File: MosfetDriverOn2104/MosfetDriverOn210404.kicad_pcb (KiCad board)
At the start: 2 copper layers, 93.5 x 94.9 mm, 88 parts, among them J1 I2C HDR, J10 ENCODER HDR, J11 CROSS CONN, J12 motor, J2 AVR-ISP-6, J3 I2C HDR, J4 Screw_Terminal_01x02, J5 I2C HDR, J6 UART HDR, J7 5V HDR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

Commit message: check
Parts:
- moved R8 29.9 mm to (198.9, 83.5)
- moved R9 28.0 mm to (194.8, 82.1)
- moved R7 26.0 mm to (192.3, 79.3)
- moved R12 25.6 mm to (189.4, 76.5)
- moved R11 25.1 mm to (186.8, 73.5)
- moved C1 2.67 mm to (122.6, 93.3)
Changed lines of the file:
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@@
   )
   (module Capacitor_SMD:CP_Elec_8x6.2 (layer F.Cu)
-    (at 125.044564 94.432498 320)
+    (at 122.631564 93.289498 320)
     (descr "SMT capacitor, aluminium electrolytic, 8x6.2, Nichicon ")
     (tags "Capacitor Electrolytic")
@@
     (pad 2 thru_hole circle (at -5.08 -6.35 235) (size 3.556 3.556) (drill 3.556) (layers *.Cu *.Mask)
       (net 8 VCC))
-    (pad 2 thru_hole circle (at 0 -6.35 235) (size 3.556 3.556) (drill 3.556) (layers *.Cu *.Mask)
+    (pad 2 thru_hole circle (at 0 -6.349999 235) (size 3.556 3.556) (drill 3.556) (layers *.Cu *.Mask)
       (net 8 VCC))
   )
@@
     (fp_line (start 5.334 -3.048) (end -5.334 -3.048) (layer F.SilkS) (width 0.15))
     (fp_line (start 5.334 0) (end 5.334 -3.048) (layer F.SilkS) (width 0.15))
-    (pad 2 thru_hole circle (at 0 -6.35 235) (size 3.556 3.556) (drill 3.556) (layers *.Cu *.Mask)
+    (pad 2 thru_hole circle (at 0 -6.349999 235) (size 3.556 3.556) (drill 3.556) (layers *.Cu *.Mask)
       (net 42 /M1))
     (pad 2 thru_hole circle (at -5.08 -6.35 235) (size 3.556 3.556) (drill 3.556) (layers *.Cu *.Mask)
@@
     (pad 2 thru_hole circle (at -5.08 -6.35 35) (size 3.556 3.556) (drill 3.556) (layers *.Cu *.Mask)
       (net 8 VCC))
-    (pad 2 thru_hole circle (at 0 -6.35 35) (size 3.556 3.556) (drill 3.556) (layers *.Cu *.Mask)
+    (pad 2 thru_hole circle (at 0 -6.349999 35) (size 3.556 3.556) (drill 3.556) (layers *.Cu *.Mask)
       (net 8 VCC))
   )
@@
     (fp_line (start 5.334 -3.048) (end -5.334 -3.048) (layer F.SilkS) (width 0.15))
     (fp_line (start 5.334 0) (end 5.334 -3.048) (layer F.SilkS) (width 0.15))
-    (pad 2 thru_hole circle (at 0 -6.35 35) (size 3.556 3.556) (drill 3.556) (layers *.Cu *.Mask)
+    (pad 2 thru_hole circle (at 0 -6.349999 35) (size 3.556 3.556) (drill 3.556) (layers *.Cu *.Mask)
       (net 41 /M2))
     (pad 2 thru_hole circle (at -5.08 -6.35 35) (size 3.556 3.556) (drill 3.556) (layers *.Cu *.Mask)
@@
   )
   (module Resistor_SMD:R_2512_6332Metric (layer B.Cu)
-    (at 169.074288 90.891129 220)
+    (at 192.342471 79.334084 220)
     (descr "Resistor SMD 2512 (6332 Metric), square (rectangular) end terminal, IPC_7351 nominal, (Body size source: http://www.tortai-tech.com/upload/download/2011102023233369053.pdf), generated with kicad-footprint-generator")
     (tags resistor)
@@
   )
   (module Resistor_SMD:R_2512_6332Metric (layer B.Cu)
-    (at 170.393841 92.436481 220)
+    (at 198.944529 83.479916 220)
     (descr "Resistor SMD 2512 (6332 Metric), square (rectangular) end terminal, IPC_7351 nominal, (Body size source: http://www.tortai-tech.com/upload/download/2011102023233369053.pdf), generated with kicad-footprint-generator")
     (tags resistor)
@@
   )
   (module Resistor_SMD:R_2512_6332Metric (layer B.Cu)
-    (at 167.667309 89.087565 220)
+    (at 194.755471 82.128084 220)
     (descr "Resistor SMD 2512 (6332 Metric), square (rectangular) end terminal, IPC_7351 nominal, (Body size source: http://www.tortai-tech.com/upload/download/2011102023233369053.pdf), generated with kicad-footprint-generator")
     (tags resistor)
@@
   )
   (module Resistor_SMD:R_2512_6332Metric (layer B.Cu)
-    (at 164.726184 85.587138 220)
+    (at 186.754471 73.492084 220)
     (descr "Resistor SMD 2512 (6332 Metric), square (rectangular) end terminal, IPC_7351 nominal, (Body size source: http://www.tortai-tech.com/upload/download/2011102023233369053.pdf), generated with kicad-footprint-generator")
     (tags resistor)
@@
   )
   (module Resistor_SMD:R_2512_6332Metric (layer B.Cu)
-    (at 166.113966 87.241028 220)
+    (at 189.421471 76.540084 220)
     (descr "Resistor SMD 2512 (6332 Metric), square (rectangular) end terminal, IPC_7351 nominal, (Body size source: http://www.tortai-tech.com/upload/download/2011102023233369053.pdf), generated with kicad-footprint-generator")
     (tags resistor)

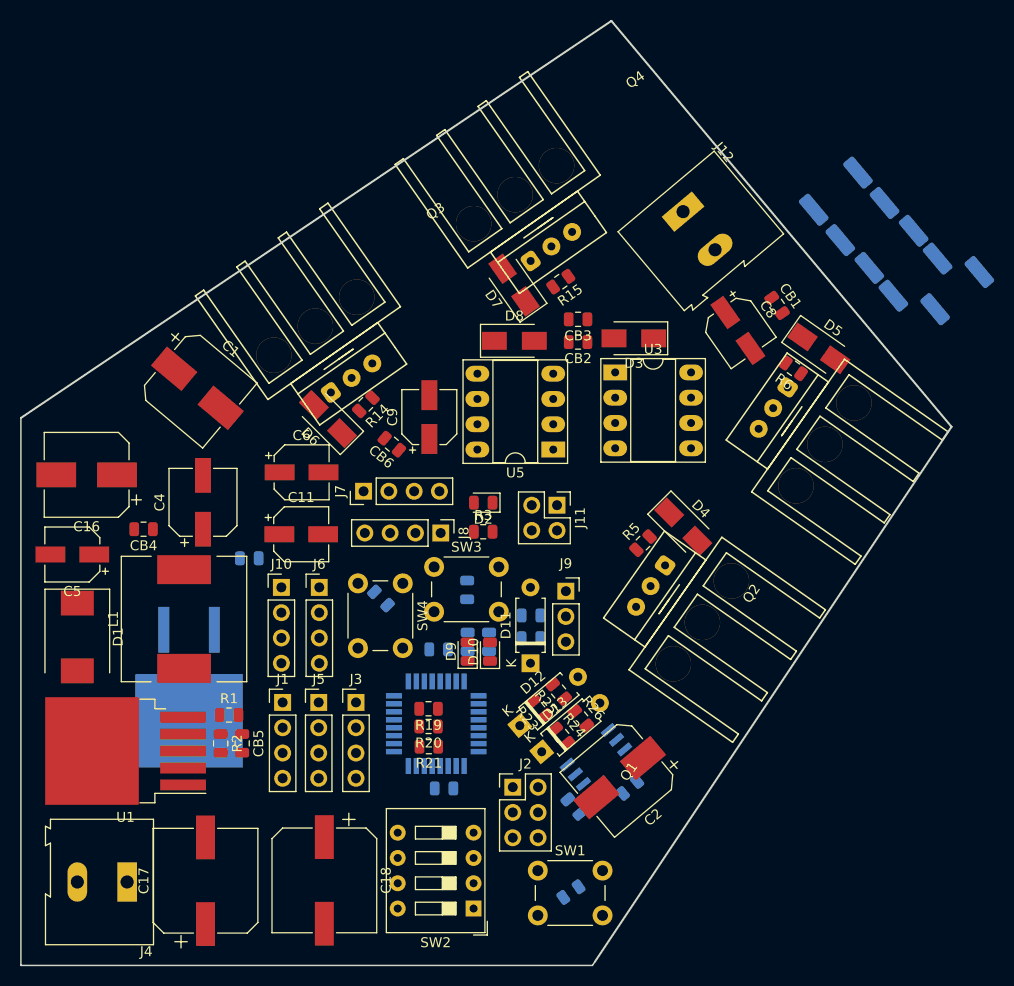
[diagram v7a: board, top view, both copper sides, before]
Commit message: longest diagonals for pcb: 89mm on y axis and 84mm on x axis
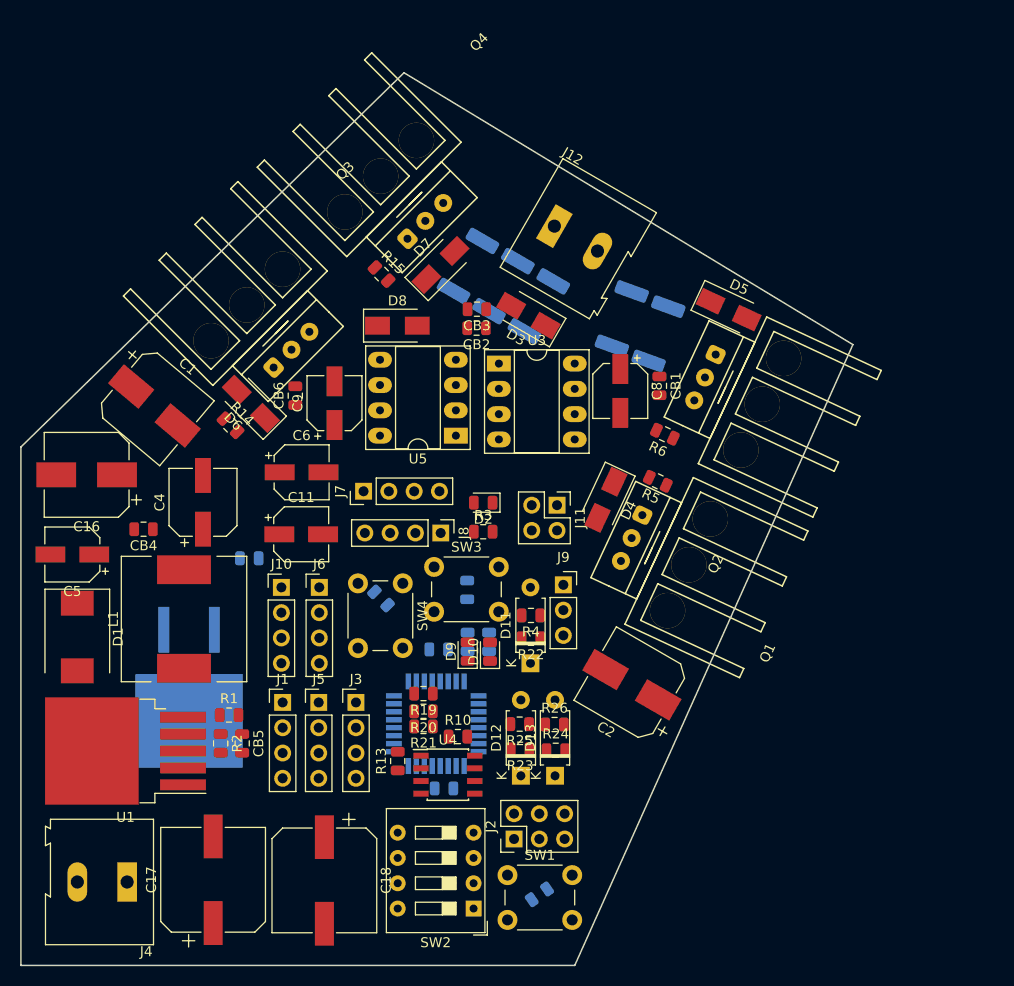
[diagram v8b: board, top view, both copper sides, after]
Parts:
- R10, R13, R22, R4, U4: moved to F.Cu
- moved R11 37.7 mm to (149.8, 81.0), turned to 240 degrees
- moved R12 36.6 mm to (153.4, 83.0), turned to 240 degrees
- moved R7 35.9 mm to (156.9, 85.1), turned to 240 degrees
- moved R8 30.3 mm to (168.9, 87.8), turned to 250 degrees
- moved R9 29.8 mm to (165.3, 86.3), turned to 250 degrees
- moved R13 18.3 mm to (142.7, 130.7), turned to 90 degrees
- moved R10 18.0 mm to (148.8, 128.3), turned to 0 degrees
- moved R15 18.0 mm to (141.1, 81.8), turned to 315 degrees
- moved U4 15.3 mm to (147.8, 132.1), turned to 0 degrees
- moved R6 14.5 mm to (169.6, 97.9), turned to 155 degrees
- moved CB1 14.3 mm to (169.0, 93.0), turned to 270 degrees
- moved R14 13.8 mm to (126.0, 97.0), turned to 315 degrees
- moved C8 13.3 mm to (165.1, 93.6), turned to 270 degrees
- moved J12 13.0 mm to (158.5, 77.0), turned to 330 degrees
- moved Q4 12.9 mm to (145.5, 76.5), turned to 45 degrees
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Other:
- board size 93.5 x 94.9 mm -> 83.6 x 89.7 mm
